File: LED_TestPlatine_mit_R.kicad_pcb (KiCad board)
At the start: 2 copper layers, 11 x 15 mm, 4 parts, among them Y1 XEGARY-H2-0000-000-000000K2001

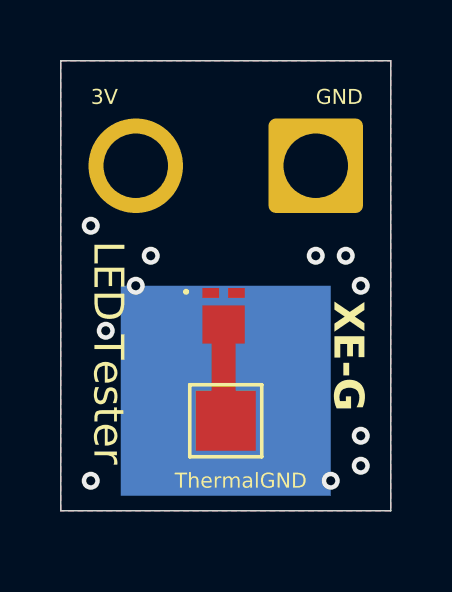
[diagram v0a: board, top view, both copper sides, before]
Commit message: added resistor to respective files
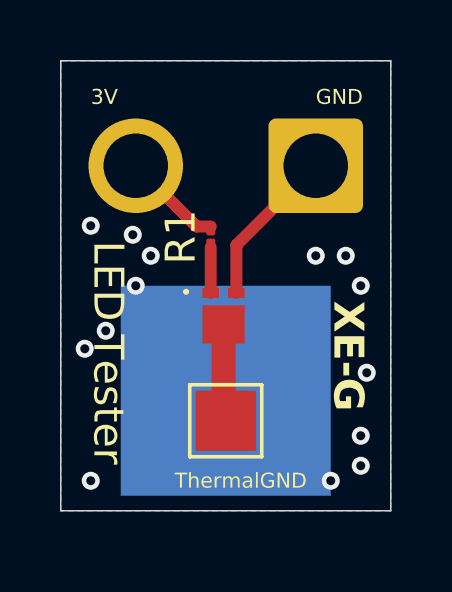
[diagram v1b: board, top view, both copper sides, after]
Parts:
- added R1: 200, Resistor_SMD:R_01005_0402Metric, F.Cu at (130.0, 70.9)
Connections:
- Y1 pad 1: +3V0 -> Net-(Y1-A)
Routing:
- net GND: track 0.00 -> 5.34 mm
- net +3V0: track 0.00 -> 3.34 mm
- net Net-(Y1-A): track 0.00 -> 1.52 mm
- net ThermalGround: vias 11 -> 14
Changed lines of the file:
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@@
+		)
+	)
+	(footprint "Resistor_SMD:R_01005_0402Metric"
+		(layer "F.Cu")
+		(at 130 70.875 90)
+		(descr "Resistor SMD 01005 (0402 Metric), square (rectangular) end terminal, IPC-7351 nominal, (Body size source: http://www.vishay.com/docs/20056/crcw01005e3.pdf)")
+		(tags "resistor")
+		(property "Reference" "R1"
+			(at 0 -1 90)
+			(layer "F.SilkS")
+			(effects
+				(font
+					(size 1 1)
+					(thickness 0.15)
+				)
+			)
+		)
+		(property "Value" "200"
+			(at 0 1 90)
+			(layer "F.Fab")
+			(effects
+				(font
+					(size 1 1)
+					(thickness 0.15)
+				)
+			)
+		)
+		(property "Datasheet" ""
+			(at 0 0 90)
+			(layer "F.Fab")
+			(hide yes)
+			(effects
+				(font
+					(size 1.27 1.27)
+				)
+			)
+		)
+		(property "Description" "Resistor"
+			(at 0 0 90)
+			(layer "F.Fab")
+			(hide yes)
+			(effects
+				(font
+					(size 1.27 1.27)
+				)
+			)
+		)
+		(property "KiLib_Generator" "SMD_2terminal_chip_molded"
+			(at 0 0 90)
+			(layer "F.SilkS")
+			(hide yes)
+			(effects
+				(font
+					(size 1 1)
+					(thickness 0.15)
+				)
+			)
+		)
+		(property ki_fp_filters "R_*")
+		(sheetname "/")
+		(sheetfile "LED_TestPlatine.kicad_sch")
+		(units
+			(unit
+				(name "A")
+				(pins "1" "2")
+			)
+		)
+		(attr smd)
+		(duplicate_pad_numbers_are_jumpers no)
+		(fp_rect
+			(start -0.6 -0.3)
+			(end 0.6 0.3)
+			(stroke
+				(width 0.05)
+				(type solid)
+			)
+			(fill no)
+			(layer "F.CrtYd")
+		)
+		(fp_rect
+			(start -0.2 -0.1)
+			(end 0.2 0.1)
+			(stroke
+				(width 0.1)
+				(type solid)
+			)
+			(fill no)
+			(layer "F.Fab")
+		)
+		(fp_text user "${REFERENCE}"
+			(at 0 -0.62 90)
+			(layer "F.Fab")
+			(effects
+				(font
+					(size 0.25 0.25)
+					(thickness 0.04)
+				)
+			)
+		)
+		(pad "" smd roundrect
+			(at -0.275 0 90)
+			(size 0.27 0.27)
+			(layers "F.Paste")
+			(roundrect_rratio 0.25)
+		)
+		(pad "" smd roundrect
+			(at 0.275 0 90)
+			(size 0.27 0.27)
+			(layers "F.Paste")
+			(roundrect_rratio 0.25)
+		)
+		(pad "1" smd roundrect
+			(at -0.25 0 90)
+			(size 0.4 0.3)
+			(layers "F.Cu" "F.Mask")
+			(roundrect_rratio 0.25)
+			(net "Net-(Y1-A)")
+			(pintype "passive")
+		)
+		(pad "2" smd roundrect
+			(at 0.25 0 90)
+			(size 0.4 0.3)
+			(layers "F.Cu" "F.Mask")
+			(roundrect_rratio 0.25)
+			(net "+3V0")
+			(pintype "passive")
+		)
+		(embedded_fonts no)
+		(model "${KICAD10_3DMODEL_DIR}/Resistor_SMD.3dshapes/R_01005_0402Metric.step"
+			(offset
+				(xyz 0 0 0)
+			)
+			(scale
+				(xyz 1 1 1)
+			)
+			(rotate
+				(xyz 0 0 0)
+			)
 		)
 	)
@@
 			(size 0.33 0.555)
 			(layers "F.Cu" "F.Mask" "F.Paste")
-			(net "+3V0")
+			(net "Net-(Y1-A)")
 			(pinfunction "A_1")
 			(pintype "passive")
@@
 	)
 	(via
+		(at 135.2 75.4)
+		(size 0.6)
+		(drill 0.3)
+		(layers "F.Cu" "B.Cu")
+		(free yes)
+		(net "ThermalGround")
+	)
+	(via
+		(at 127.4 70.8)
+		(size 0.6)
+		(drill 0.3)
+		(layers "F.Cu" "B.Cu")
+		(free yes)
+		(net "ThermalGround")
+	)
+	(via
+		(at 125.8 74.6)
+		(size 0.6)
+		(drill 0.3)
+		(layers "F.Cu" "B.Cu")
+		(free yes)
+		(net "ThermalGround")
+	)
+	(via
 		(at 127.5 72.5)
 		(size 0.6)
@@
 		(net "ThermalGround")
 	)
+	(segment
+		(start 130.855 71.145)
+		(end 133.5 68.5)
+		(width 0.4)
+		(layer "F.Cu")
+		(net "GND")
+	)
+	(segment
+		(start 130.855 72.74)
+		(end 130.855 71.145)
+		(width 0.4)
+		(layer "F.Cu")
+		(net "GND")
+	)
+	(segment
+		(start 129.525 70.525)
+		(end 130 70.525)
+		(width 0.4)
+		(layer "F.Cu")
+		(net "+3V0")
+	)
+	(segment
+		(start 127.5 68.5)
+		(end 129.525 70.525)
+		(width 0.4)
+		(layer "F.Cu")
+		(net "+3V0")
+	)
+	(segment
+		(start 130 72.74)
+		(end 130 71.225)
+		(width 0.4)
+		(layer "F.Cu")
+		(net "Net-(Y1-A)")
+	)
 	(zone

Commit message: moved resistor to the correct board file
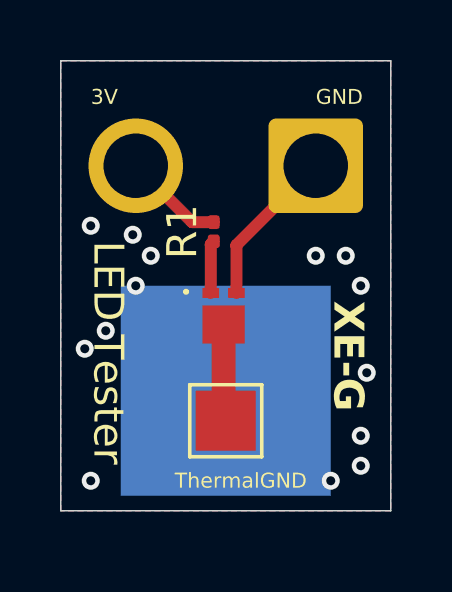
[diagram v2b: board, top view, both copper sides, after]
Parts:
- R1: value 200 -> 50; footprint Resistor_SMD:R_01005_0402Metric -> Resistor_SMD:R_0201_0603Metric
- moved R1 0.20 mm to (130.1, 70.7)
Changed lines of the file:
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@@
 		)
 	)
-	(footprint "Resistor_SMD:R_01005_0402Metric"
-		(layer "F.Cu")
-		(at 130 70.875 90)
-		(descr "Resistor SMD 01005 (0402 Metric), square (rectangular) end terminal, IPC-7351 nominal, (Body size source: http://www.vishay.com/docs/20056/crcw01005e3.pdf)")
+	(footprint "Resistor_SMD:R_0201_0603Metric"
+		(layer "F.Cu")
+		(at 130.1 70.7 90)
+		(descr "Resistor SMD 0201 (0603 Metric), square (rectangular) end terminal, IPC-7351 nominal, (Body size source: https://www.vishay.com/docs/20052/crcw0201e3.pdf)")
 		(tags "resistor")
 		(property "Reference" "R1"
-			(at 0 -1 90)
-			(layer "F.SilkS")
-			(effects
-				(font
-					(size 1 1)
-					(thickness 0.15)
-				)
-			)
-		)
-		(property "Value" "200"
-			(at 0 1 90)
+			(at 0 -1.05 90)
+			(layer "F.SilkS")
+			(effects
+				(font
+					(size 1 1)
+					(thickness 0.15)
+				)
+			)
+		)
+		(property "Value" "50"
+			(at 0 1.05 90)
 			(layer "F.Fab")
 			(effects
@@
 		(duplicate_pad_numbers_are_jumpers no)
 		(fp_rect
-			(start -0.6 -0.3)
-			(end 0.6 0.3)
+			(start -0.7 -0.35)
+			(end 0.7 0.35)
 			(stroke
 				(width 0.05)
@@
 		)
 		(fp_rect
-			(start -0.2 -0.1)
-			(end 0.2 0.1)
+			(start -0.3 -0.15)
+			(end 0.3 0.15)
 			(stroke
 				(width 0.1)
@@
 		)
 		(fp_text user "${REFERENCE}"
-			(at 0 -0.62 90)
+			(at 0 -0.68 90)
 			(layer "F.Fab")
 			(effects
@@
 		)
 		(pad "" smd roundrect
-			(at -0.275 0 90)
-			(size 0.27 0.27)
+			(at -0.345 0 90)
+			(size 0.318 0.36)
 			(layers "F.Paste")
 			(roundrect_rratio 0.25)
 		)
 		(pad "" smd roundrect
-			(at 0.275 0 90)
-			(size 0.27 0.27)
+			(at 0.345 0 90)
+			(size 0.318 0.36)
 			(layers "F.Paste")
 			(roundrect_rratio 0.25)
 		)
 		(pad "1" smd roundrect
-			(at -0.25 0 90)
-			(size 0.4 0.3)
+			(at -0.32 0 90)
+			(size 0.46 0.4)
 			(layers "F.Cu" "F.Mask")
 			(roundrect_rratio 0.25)
@@
 		)
 		(pad "2" smd roundrect
-			(at 0.25 0 90)
-			(size 0.4 0.3)
+			(at 0.32 0 90)
+			(size 0.46 0.4)
 			(layers "F.Cu" "F.Mask")
 			(roundrect_rratio 0.25)
@@
 		)
 		(embedded_fonts no)
-		(model "${KICAD10_3DMODEL_DIR}/Resistor_SMD.3dshapes/R_01005_0402Metric.step"
+		(model "${KICAD10_3DMODEL_DIR}/Resistor_SMD.3dshapes/R_0201_0603Metric.step"
 			(offset
 				(xyz 0 0 0)
@@
 	)
 	(segment
+		(start 130 72.74)
+		(end 130 71.12)
+		(width 0.4)
+		(layer "F.Cu")
+		(net "Net-(Y1-A)")
+	)
+	(segment
+		(start 130 71.12)
+		(end 130.1 71.02)
+		(width 0.4)
+		(layer "F.Cu")
+		(net "Net-(Y1-A)")
+	)
+	(segment
+		(start 130.1 70.38)
+		(end 129.38 70.38)
+		(width 0.4)
+		(layer "F.Cu")
+		(net "+3V0")
+	)
+	(segment
+		(start 129.38 70.38)
+		(end 127.5 68.5)
+		(width 0.4)
+		(layer "F.Cu")
+		(net "+3V0")
+	)
+	(segment
 		(start 130.428 73.79)
 		(end 130.428 76.928)
@@
 		(net "GND")
 	)
-	(segment
-		(start 129.525 70.525)
-		(end 130 70.525)
-		(width 0.4)
-		(layer "F.Cu")
-		(net "+3V0")
-	)
-	(segment
-		(start 127.5 68.5)
-		(end 129.525 70.525)
-		(width 0.4)
-		(layer "F.Cu")
-		(net "+3V0")
-	)
-	(segment
-		(start 130 72.74)
-		(end 130 71.225)
-		(width 0.4)
-		(layer "F.Cu")
-		(net "Net-(Y1-A)")
-	)
 	(zone
